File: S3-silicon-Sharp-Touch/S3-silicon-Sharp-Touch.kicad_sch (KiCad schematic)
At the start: 64 parts, among them IC1 ESP32-S3FN8, J2 Conn_01x06_Socket, J3 Conn_01x11_Socket, J5 FH52-10S-0.5SH_99, J6 5024260810, J7 S2B-PH-SM4-TB_LF__SN_, J9 USB_C_Receptacle_USB2.0, Q3 MMBT3904, Q3 Si2301CDS, Q4 MMBT3904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

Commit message: 1.0 sent to fabrication
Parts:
- R1, R11: LCSC C5123581 -> C25804
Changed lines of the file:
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@@
       (effects (font (size 1.27 1.27)) hide)
     )
-    (property "LCSC" "C5123581" (at 115.57 168.91 90)
+    (property "LCSC" "C25804" (at 115.57 168.91 90)
       (effects (font (size 1.27 1.27)) hide)
     )
@@
       (effects (font (size 1.27 1.27)) hide)
     )
-    (property "LCSC" "C5123581" (at 115.57 156.21 90)
-      (effects (font (size 1.27 1.27)) hide)
-    )
+    (property "LCSC" "C25804" (at 115.57 156.21 90)
+      (effects (font (size 1.27 1.27)) hide)
+    )

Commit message: Move touch 2 mm right
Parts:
- C3: LCSC C3846795 -> C327087
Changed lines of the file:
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@@
       (effects (font (size 1.27 1.27)) hide)
     )
-    (property "LCSC" "C3846795" (at 207.01 182.88 0)
+    (property "LCSC" "C327087" (at 207.01 182.88 0)
       (effects (font (size 1.27 1.27)) hide)
     )
@@
       (effects (font (size 1.27 1.27)) hide)
     )
-    (property "LCSC" "C3846795" (at 147.32 78.74 0)
+    (property "LCSC" "C327087" (at 147.32 78.74 0)
       (effects (font (size 1.27 1.27)) hide)
     )
@@
       (effects (font (size 1.27 1.27)) hide)
     )
-    (property "LCSC" "C3846795" (at 238.76 53.34 0)
+    (property "LCSC" "C327087" (at 238.76 53.34 0)
       (effects (font (size 1.27 1.27)) hide)
     )
@@
       (effects (font (size 1.27 1.27)) hide)
     )
-    (property "LCSC" "C3846795" (at 167.64 78.74 0)
-      (effects (font (size 1.27 1.27)) hide)
-    )
+    (property "LCSC" "C327087" (at 167.64 78.74 0)
+      (effects (font (size 1.27 1.27)) hide)
+    )

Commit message: Corrections heading to Rev 1.1 (Bottom ROW of Touch RIGHT!)
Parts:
- removed TP2: RTC_INT, TestPoint:TestPoint_Pad_1.5x1.5mm, symbol Connector:TestPoint
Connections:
- net SCL: now also IC1.13 (GPIO8); no longer IC1.12 (GPIO7)
- net SDA: now also IC1.12 (GPIO7); no longer IC1.13 (GPIO8)
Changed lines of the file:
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@@
   (junction (at 238.76 49.53) (diameter 0) (color 0 0 0 0)
   )
-  (junction (at 38.1 41.91) (diameter 0) (color 0 0 0 0)
-  )
   (junction (at 176.53 50.8) (diameter 0) (color 0 0 0 0)
   )
@@
     (stroke (width 0) (type default))
   )
-  (wire (pts (xy 33.02 41.91) (xy 38.1 41.91))
-    (stroke (width 0) (type default))
-  )
   (wire (pts (xy 38.1 41.91) (xy 38.1 38.1))
     (stroke (width 0) (type default))
@@
     (effects (font (size 1.27 1.27) (thickness 0.254) bold (color 255 153 0 1)) (justify right bottom))
   )
+  (label "SCL" (at 186.69 120.65 180) (fields_autoplaced)
+    (effects (font (size 1.27 1.27) (thickness 0.254) bold (color 0 194 0 1)) (justify right bottom))
+  )
   (label "IO17" (at 214.63 146.05 270) (fields_autoplaced)
     (effects (font (size 1.27 1.27)) (justify right bottom))
   )
+  (label "SDA" (at 186.69 118.11 180) (fields_autoplaced)
+    (effects (font (size 1.27 1.27) (thickness 0.254) bold (color 0 194 0 1)) (justify right bottom))
+  )
   (label "RTC_SQW" (at 97.79 48.26 0) (fields_autoplaced)
     (effects (font (size 1.27 1.27)) (justify left bottom))
@@
     (effects (font (size 1.27 1.27) (thickness 0.254) bold (color 0 132 132 1)) (justify right bottom))
   )
-  (label "SCL" (at 186.69 118.11 180) (fields_autoplaced)
-    (effects (font (size 1.27 1.27) (thickness 0.254) bold (color 0 194 0 1)) (justify right bottom))
-  )
   (label "RTS" (at 52.07 205.74 180) (fields_autoplaced)
     (effects (font (size 1.27 1.27)) (justify right bottom))
@@
     (effects (font (size 1.27 1.27) (thickness 0.254) bold (color 72 72 72 1)) (justify right bottom))
   )
-  (label "SDA" (at 186.69 120.65 180) (fields_autoplaced)
-    (effects (font (size 1.27 1.27) (thickness 0.254) bold (color 0 194 0 1)) (justify right bottom))
-  )
   (label "USB_D-" (at 219.71 146.05 270) (fields_autoplaced)
     (effects (font (size 1.27 1.27)) (justify right bottom))
@@
         )
       )
-    )
-  )
-  (symbol (lib_id "Connector:TestPoint") (at 33.02 41.91 0) (mirror y) (unit 1)
-    (in_bom yes) (on_board yes) (dnp no)
-    (property "Reference" "TP2" (at 34.29 39.37 0)
-      (effects (font (size 1.27 1.27)) (justify right))
-    )
-    (property "Value" "RTC_INT" (at 34.417 40.3102 0)
-      (effects (font (size 1.27 1.27)) (justify right) hide)
-    )
-    (property "Footprint" "TestPoint:TestPoint_Pad_1.5x1.5mm" (at 29.21 45.72 0)
-      (effects (font (size 1.27 1.27)) hide)
-    )
-    (property "Datasheet" "~" (at 27.94 41.91 0)
-      (effects (font (size 1.27 1.27)) hide)
-    )
-    (pin "1")
-    (instances
-      (project "S3-silicon-Sharp-Touch"
-        (path "/e6751642-eada-4b92-b3bd-08d265514654"
-          (reference "TP2") (unit 1)
-        )
-      )

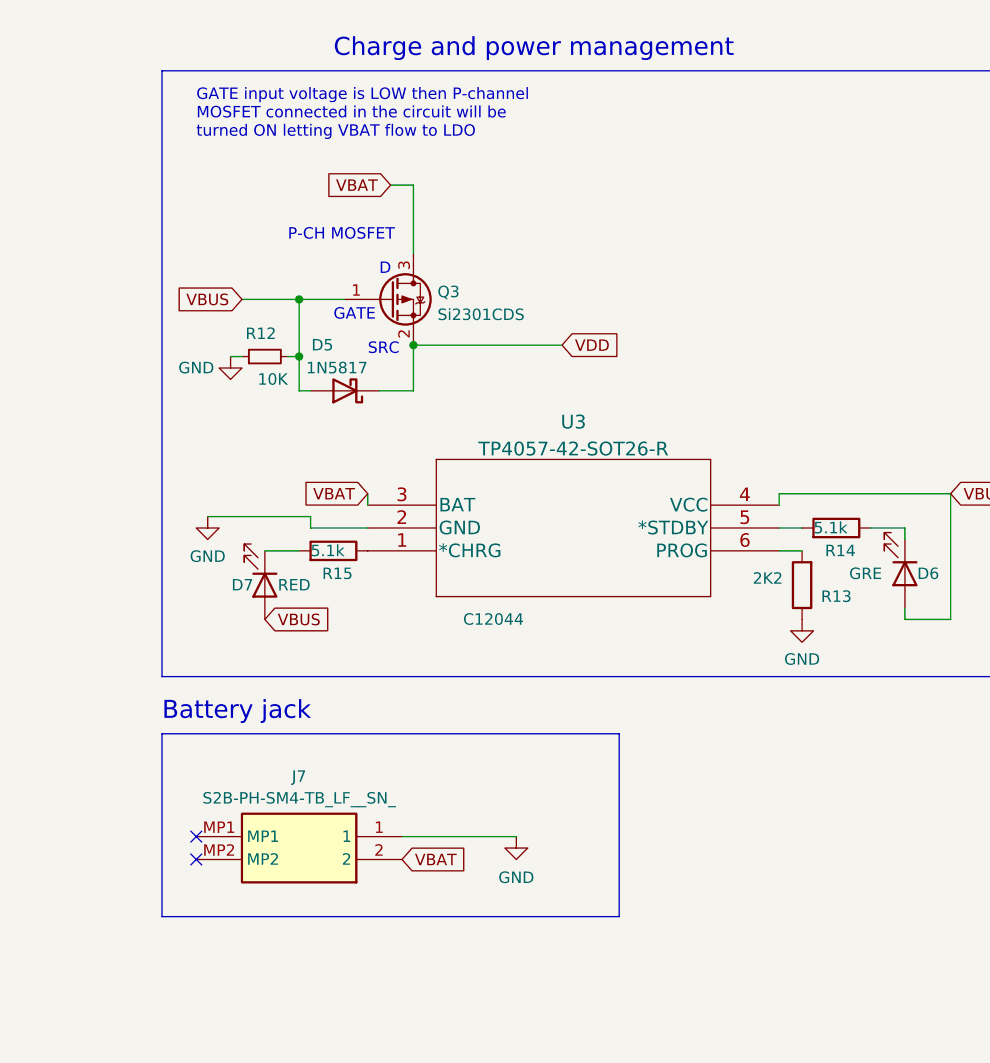
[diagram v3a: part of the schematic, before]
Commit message: Update TOUCH pinout in PCBs
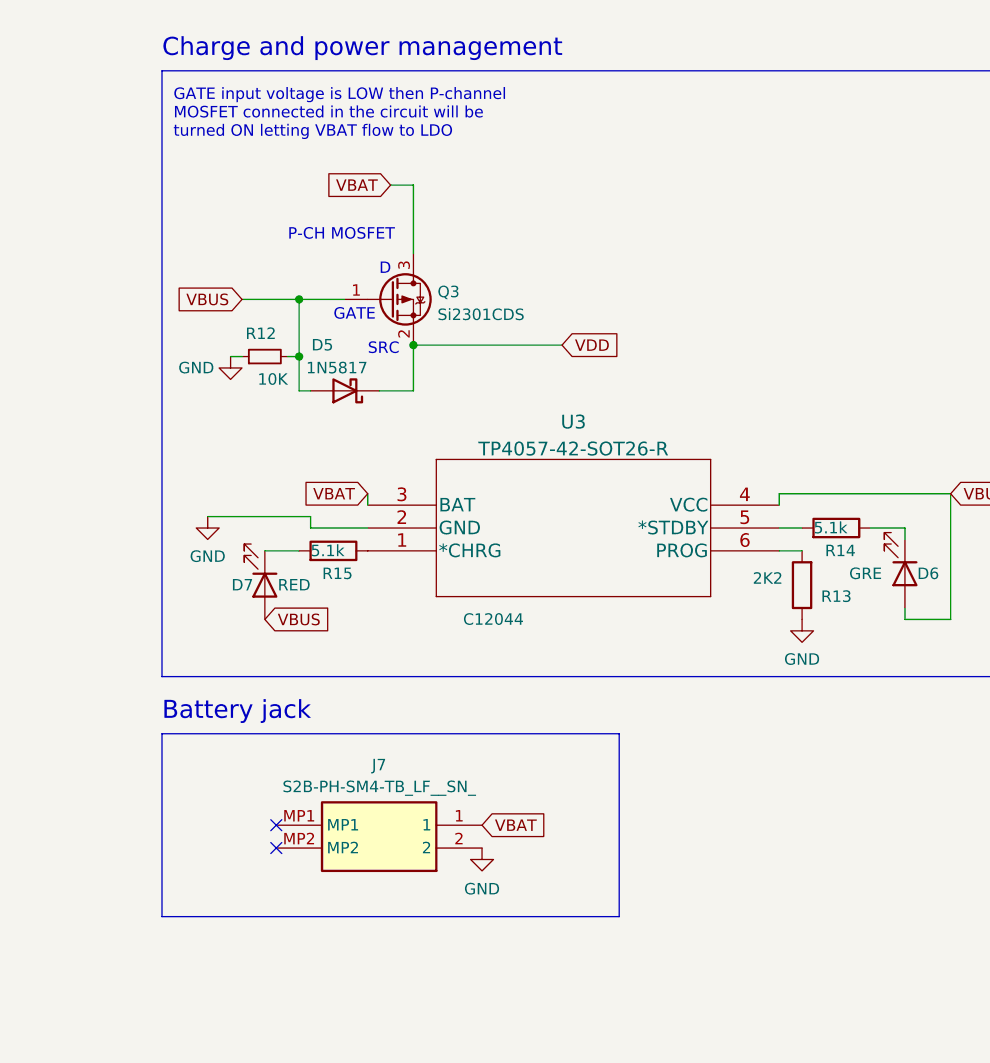
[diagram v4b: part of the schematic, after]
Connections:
- net GND: now also J7.2; no longer J7.1
- net VBAT: now also J7.1; no longer J7.2
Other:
- moved on the sheet: J7
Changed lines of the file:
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@@
   (no_connect (at 237.49 102.87))
   (no_connect (at 219.71 67.31))
-  (no_connect (at 304.8 107.95))
+  (no_connect (at 313.69 106.68))
   (no_connect (at 62.23 116.84))
   (no_connect (at 237.49 123.19))
@@
   (no_connect (at 237.49 113.03))
   (no_connect (at 209.55 67.31))
-  (no_connect (at 304.8 110.49))
+  (no_connect (at 313.69 109.22))
   (no_connect (at 358.14 171.45))
   (no_connect (at 54.61 50.8))
@@
     (stroke (width 0) (type default))
   )
-  (wire (pts (xy 327.66 107.95) (xy 340.36 107.95))
-    (stroke (width 0) (type default))
-  )
   (wire (pts (xy 317.5 72.39) (xy 306.07 72.39))
     (stroke (width 0) (type default))
@@
   )
   (text "GATE input voltage is LOW then P-channel \nMOSFET connected in the circuit will be \nturned ON letting VBAT flow to LDO"
-    (at 304.8 30.48 0)
+    (at 302.26 30.48 0)
     (effects (font (size 1.27 1.27)) (justify left bottom))
   )
@@
     (effects (font (size 1.27 1.27)) (justify left bottom))
   )
-  (text "Charge and power management" (at 320.04 21.59 0)
+  (text "Charge and power management" (at 300.99 21.59 0)
     (effects (font (size 2 2)) (justify left bottom))
   )
@@
     )
   )
-  (global_label "VBAT" (shape input) (at 327.66 110.49 0) (fields_autoplaced)
-    (effects (font (size 1.27 1.27)) (justify left))
-    (property "Intersheetrefs" "${INTERSHEET_REFS}" (at 335.06 110.49 0)
-      (effects (font (size 1.27 1.27)) (justify left) hide)
-    )
-  )
   (global_label "RX" (shape input) (at 212.09 67.31 90) (fields_autoplaced)
     (effects (font (size 1.27 1.27)) (justify left))
@@
     )
   )
+  (global_label "VBAT" (shape input) (at 336.55 106.68 0) (fields_autoplaced)
+    (effects (font (size 1.27 1.27)) (justify left))
+    (property "Intersheetrefs" "${INTERSHEET_REFS}" (at 343.95 106.68 0)
+      (effects (font (size 1.27 1.27)) (justify left) hide)
+    )
+  )
   (global_label "VBUS" (shape input) (at 309.88 48.26 180) (fields_autoplaced)
     (effects (font (size 1.27 1.27)) (justify right))
@@
     )
   )
-  (symbol (lib_id "BATTERY:S2B-PH-SM4-TB_LF__SN_") (at 327.66 110.49 180) (unit 1)
+  (symbol (lib_id "BATTERY:S2B-PH-SM4-TB_LF__SN_") (at 336.55 109.22 180) (unit 1)
     (in_bom yes) (on_board yes) (dnp no) (fields_autoplaced)
-    (property "Reference" "J7" (at 316.23 101.2657 0)
+    (property "Reference" "J7" (at 325.12 99.9957 0)
       (effects (font (size 1.27 1.27)))
     )
-    (property "Value" "S2B-PH-SM4-TB_LF__SN_" (at 316.23 103.6899 0)
+    (property "Value" "S2B-PH-SM4-TB_LF__SN_" (at 325.12 102.4199 0)
       (effects (font (size 1.27 1.27)))
     )
-    (property "Footprint" "S2BPHSM4TBLFSN" (at 308.61 15.57 0)
+    (property "Footprint" "S2BPHSM4TBLFSN" (at 317.5 14.3 0)
       (effects (font (size 1.27 1.27)) (justify left top) hide)
     )
-    (property "Datasheet" "https://www.jst-mfg.com/product/pdf/eng/ePH.pdf" (at 308.61 -84.43 0)
+    (property "Datasheet" "https://www.jst-mfg.com/product/pdf/eng/ePH.pdf" (at 317.5 -85.7 0)
       (effects (font (size 1.27 1.27)) (justify left top) hide)
     )
-    (property "Height" "6.6" (at 308.61 -284.43 0)
+    (property "Height" "6.6" (at 317.5 -285.7 0)
       (effects (font (size 1.27 1.27)) (justify left top) hide)
     )
-    (property "Manufacturer_Name" "JST (JAPAN SOLDERLESS TERMINALS)" (at 308.61 -384.43 0)
+    (property "Manufacturer_Name" "JST (JAPAN SOLDERLESS TERMINALS)" (at 317.5 -385.7 0)
       (effects (font (size 1.27 1.27)) (justify left top) hide)
     )
-    (property "Manufacturer_Part_Number" "S2B-PH-SM4-TB(LF)(SN)" (at 308.61 -484.43 0)
+    (property "Manufacturer_Part_Number" "S2B-PH-SM4-TB(LF)(SN)" (at 317.5 -485.7 0)
       (effects (font (size 1.27 1.27)) (justify left top) hide)
     )
-    (property "LCSC" "C295747" (at 308.61 -784.43 0)
+    (property "LCSC" "C295747" (at 317.5 -785.7 0)
       (effects (font (size 1.27 1.27)) (justify left top) hide)
     )
-    (property "Mouser Part Number" "" (at 308.61 -584.43 0)
+    (property "Mouser Part Number" "" (at 317.5 -585.7 0)
       (effects (font (size 1.27 1.27)) (justify left top) hide)
     )
-    (property "Mouser Price/Stock" "" (at 308.61 -684.43 0)
+    (property "Mouser Price/Stock" "" (at 317.5 -685.7 0)
       (effects (font (size 1.27 1.27)) (justify left top) hide)
     )
-    (property "Arrow Part Number" "S2B-PH-SM4-TB(LF)(SN)" (at 308.61 -784.43 0)
+    (property "Arrow Part Number" "S2B-PH-SM4-TB(LF)(SN)" (at 317.5 -785.7 0)
       (effects (font (size 1.27 1.27)) (justify left top) hide)
     )
-    (property "Arrow Price/Stock" "https://www.arrow.com/en/products/s2b-ph-sm4-tb-lf-sn/jst-manufacturing?region=europe" (at 308.61 -884.43 0)
+    (property "Arrow Price/Stock" "https://www.arrow.com/en/products/s2b-ph-sm4-tb-lf-sn/jst-manufacturing?region=europe" (at 317.5 -885.7 0)
       (effects (font (size 1.27 1.27)) (justify left top) hide)
     )
@@
     )
   )
-  (symbol (lib_id "power:GND") (at 340.36 107.95 0) (unit 1)
+  (symbol (lib_id "power:GND") (at 336.55 109.22 0) (unit 1)
     (in_bom yes) (on_board yes) (dnp no) (fields_autoplaced)
-    (property "Reference" "#PWR034" (at 340.36 114.3 0)
+    (property "Reference" "#PWR034" (at 336.55 115.57 0)
       (effects (font (size 1.27 1.27)) hide)
     )
-    (property "Value" "GND" (at 340.36 112.5125 0)
+    (property "Value" "GND" (at 336.55 113.7825 0)
       (effects (font (size 1.27 1.27)))
     )
-    (property "Footprint" "" (at 340.36 107.95 0)
+    (property "Footprint" "" (at 336.55 109.22 0)
       (effects (font (size 1.27 1.27)) hide)
     )
-    (property "Datasheet" "" (at 340.36 107.95 0)
+    (property "Datasheet" "" (at 336.55 109.22 0)
       (effects (font (size 1.27 1.27)) hide)
     )
